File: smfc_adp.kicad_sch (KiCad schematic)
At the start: 28 parts, among them J1 Conn_01x03_Pin, J2 Conn_01x03_Pin, J3 Conn_01x04_Socket, J4 Conn_01x04_Socket, J5 Conn_01x04_Socket, U1 ADP5091

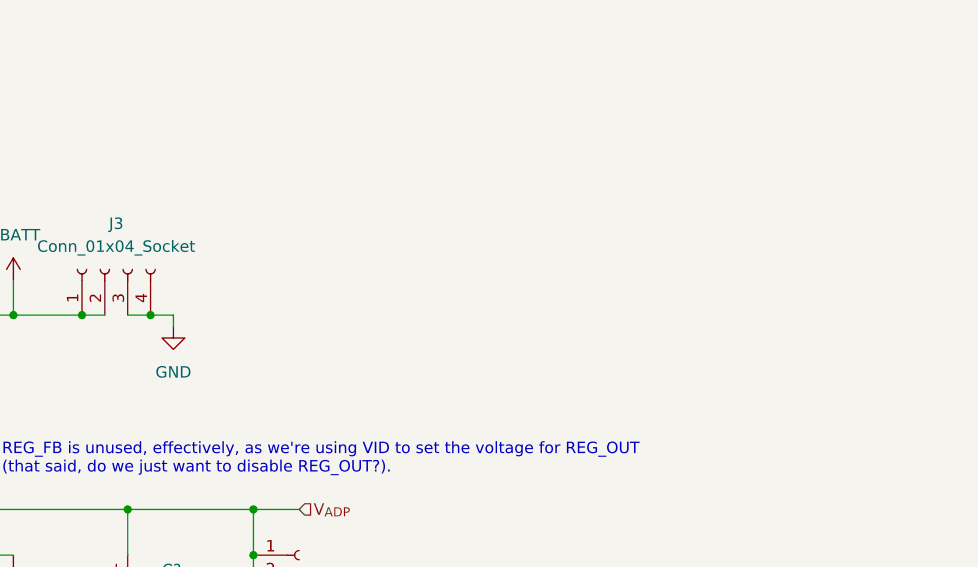
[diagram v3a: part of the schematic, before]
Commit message: Add FIXMEs, improve info on PCB silkscreen
 - Added more information about what all of the headers are on the board
 - Need to review footprints for clocks and capacitors!
 - Moved some lines around to try to get them to line up to the grid
 - Need to split the 01x04 connector for BAT/GND, annotated with FIXME
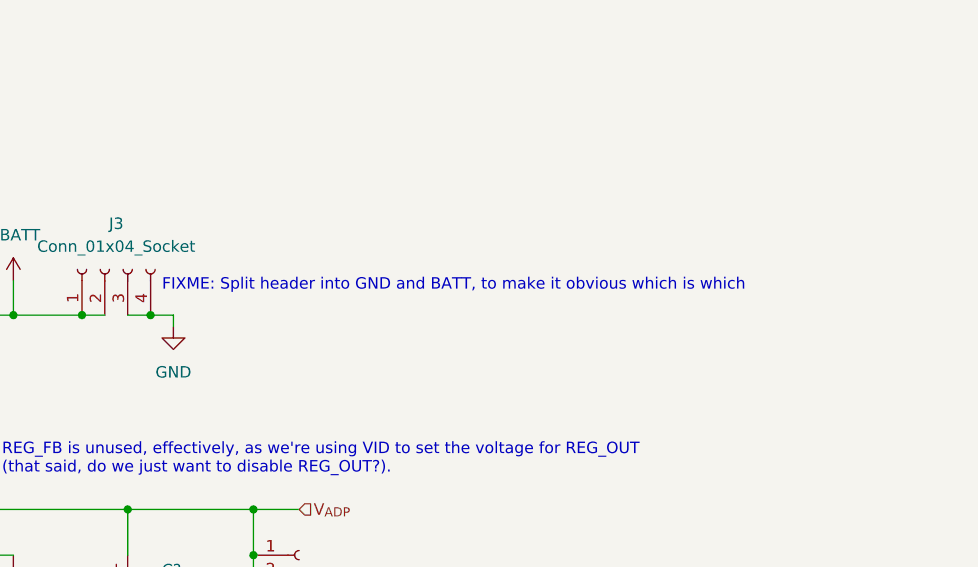
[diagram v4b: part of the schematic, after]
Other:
- note added: "FIXME: Split header into GND and BATT, to make it obvious which is which"
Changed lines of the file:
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@@
+    (effects (font (size 1.27 1.27)) (justify left bottom))
+  )
+  (text "FIXME: Split header into GND and BATT, to make it obvious which is which"
+    (at 199.39 53.34 0)
     (effects (font (size 1.27 1.27)) (justify left bottom))
   )

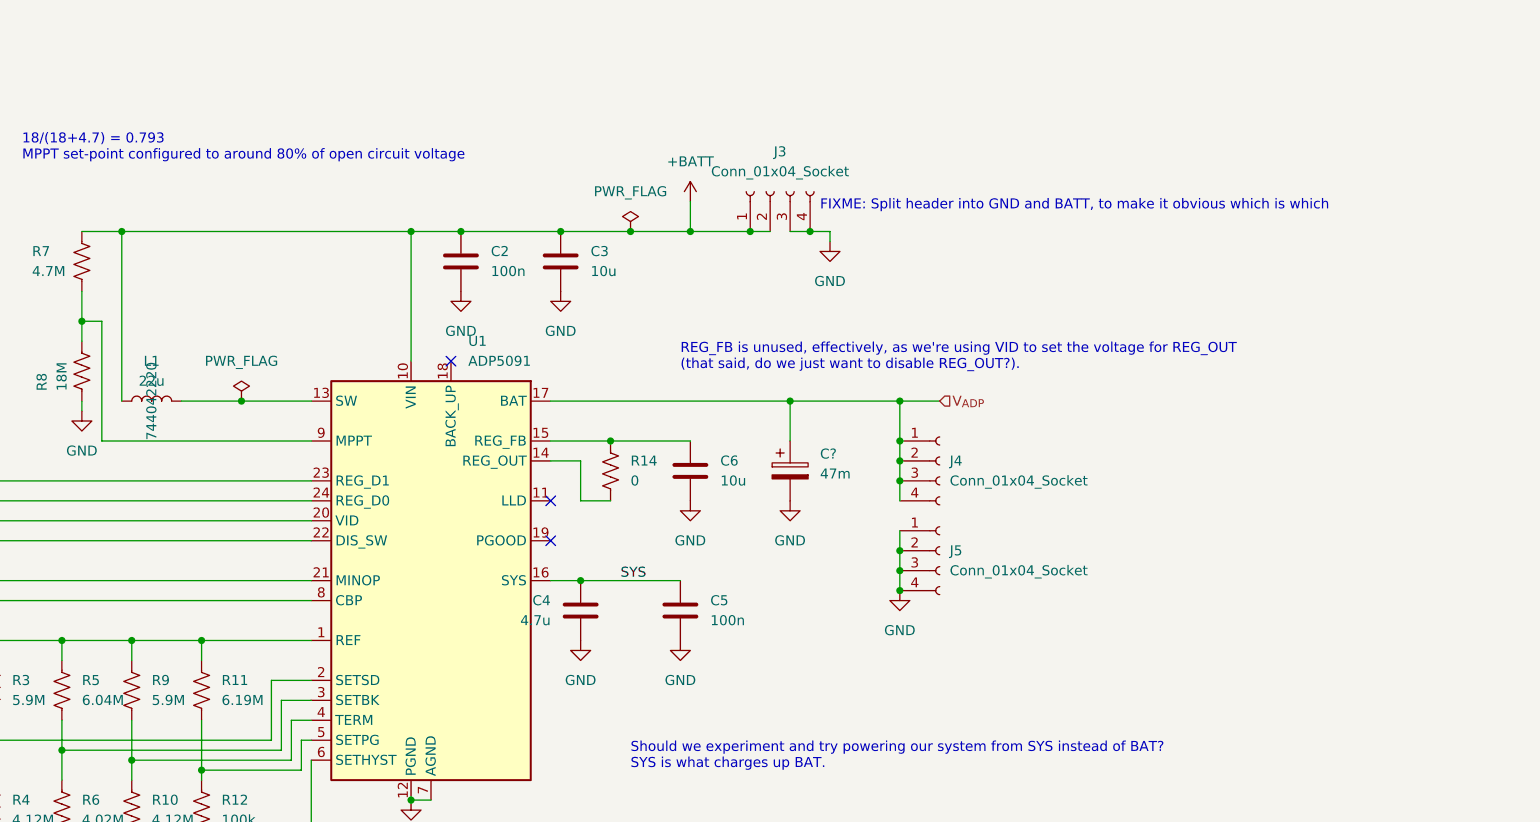
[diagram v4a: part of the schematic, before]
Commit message: Added LoRa module, lots of fixes & tweaks
 - Added loRa module as last Artemia experiment uses LoRa RFM95W
 - Added headers for debuggging purposes
 - Expanded board size to account for added hardware
 - Updated clearances to match JLCPCB manufacturing capabilities (I
   figure that if JLCPCB can fab it, anyone else can)
 - Fixed DRC issues (still need to run analysis on schematic)
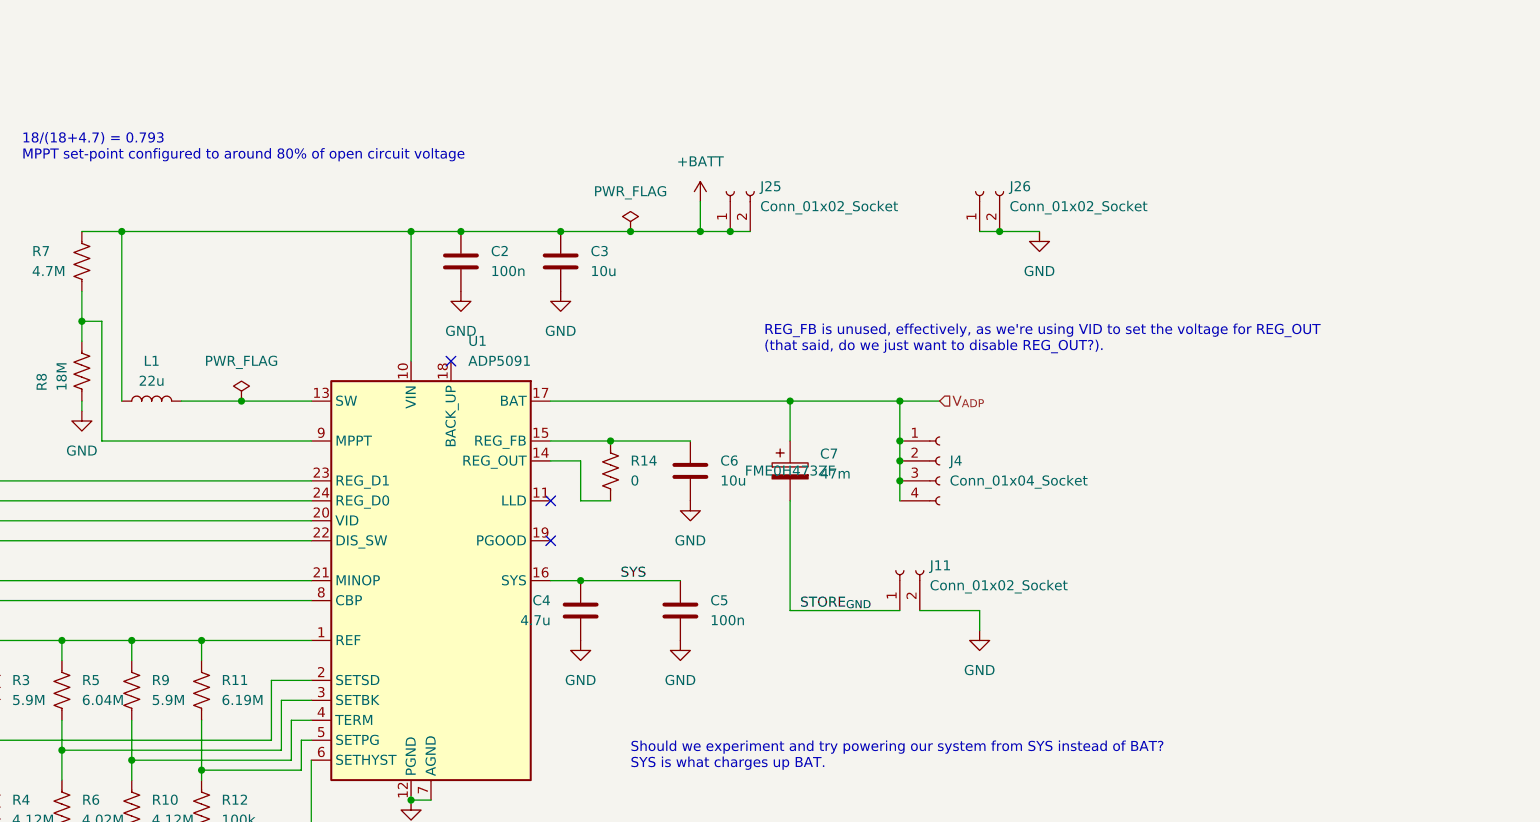
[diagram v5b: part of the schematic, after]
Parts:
- removed J3, J5: Conn_01x04_Socket, Connector_PinHeader_2.54mm:PinHeader_1x04_P2.54mm_Vertical, symbol Connector:Conn_01x04_Socket
- added J11, J25, J26: Conn_01x02_Socket, Connector_PinHeader_2.54mm:PinHeader_1x02_P2.54mm_Vertical, symbol Connector:Conn_01x02_Socket
- C7: renamed from C?; footprint Capacitor_THT:CP_Radial_D4.0mm_P1.50mm -> Marcano:KEMET_FM; Manufacturer Product Number (none) -> FME0H473ZF
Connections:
- net +BATT: now also J25.1 (Pin_1), J25.2 (Pin_2)
- net GND: now also J11.2 (Pin_2), J26.1 (Pin_1), J26.2 (Pin_2); no longer C7.2
- new net STORE_{GND}: C7.2, J11.1 (Pin_1)
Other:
- note removed: "FIXME: Split header into GND and BATT, to make it obvious which is which"
- title: Artemia: Energy Harvester -> Artemia: Energy Harvesting Subsystem
